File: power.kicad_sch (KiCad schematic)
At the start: 45 parts, among them IC302 L7805, IC303 L7805, J101 Test Points, P302 POWER, Q106 15 29, Q308 FR 32, Q503 BR 29, SW101 SW_SPDT

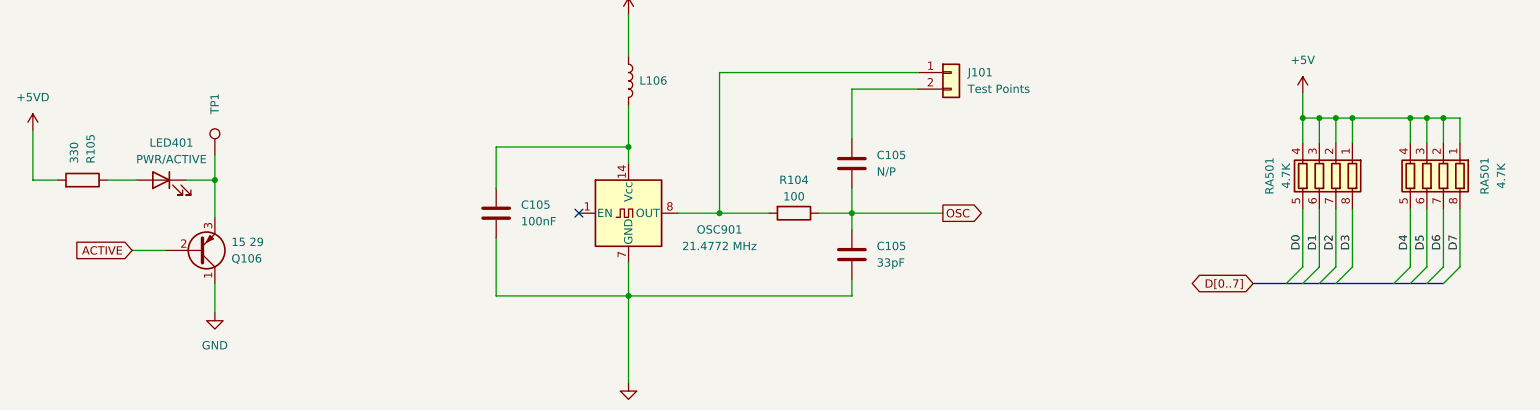
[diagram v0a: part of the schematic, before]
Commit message: Add more capacitor values, rearrange some schematics.
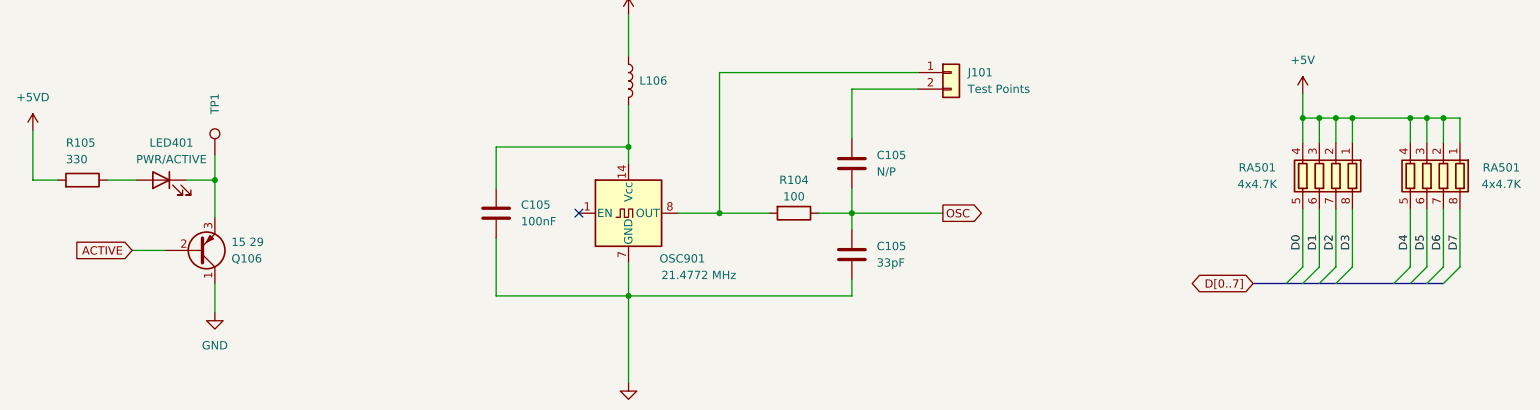
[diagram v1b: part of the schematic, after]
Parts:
- RA501: value 4.7K -> 4x4.7K
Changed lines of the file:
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@@
   (symbol (lib_id "Device:R") (at 42.545 231.775 270) (mirror x) (unit 1)
     (in_bom yes) (on_board yes) (dnp no)
-    (property "Reference" "R105" (at 43.815 229.235 0)
-      (effects (font (size 1.27 1.27)) (justify left))
-    )
-    (property "Value" "330" (at 41.275 229.235 0)
+    (property "Reference" "R105" (at 40.005 226.06 90)
+      (effects (font (size 1.27 1.27)) (justify left))
+    )
+    (property "Value" "330" (at 40.005 228.6 90)
       (effects (font (size 1.27 1.27)) (justify left))
     )
@@
   (symbol (lib_id "Oscillator:CXO_DIP14") (at 126.365 236.855 0) (unit 1)
     (in_bom yes) (on_board yes) (dnp no)
-    (property "Reference" "OSC901" (at 140.335 239.395 0)
-      (effects (font (size 1.27 1.27)))
-    )
-    (property "Value" "21.4772 MHz" (at 140.335 241.935 0)
+    (property "Reference" "OSC901" (at 134.62 243.84 0)
+      (effects (font (size 1.27 1.27)))
+    )
+    (property "Value" "21.4772 MHz" (at 137.16 246.38 0)
       (effects (font (size 1.27 1.27)))
     )
@@
   (symbol (lib_id "Device:R_Pack04") (at 232.41 231.14 180) (unit 1)
     (in_bom yes) (on_board yes) (dnp no)
-    (property "Reference" "RA501" (at 224.79 231.14 90)
-      (effects (font (size 1.27 1.27)))
-    )
-    (property "Value" "4.7K" (at 227.33 231.14 90)
+    (property "Reference" "RA501" (at 222.885 229.87 0)
+      (effects (font (size 1.27 1.27)))
+    )
+    (property "Value" "4x4.7K" (at 222.885 232.41 0)
       (effects (font (size 1.27 1.27)))
     )
@@
   (symbol (lib_id "Device:R_Pack04") (at 248.92 231.14 180) (unit 1)
     (in_bom yes) (on_board yes) (dnp no)
-    (property "Reference" "RA501" (at 257.81 231.14 90)
-      (effects (font (size 1.27 1.27)))
-    )
-    (property "Value" "4.7K" (at 260.35 231.14 90)
-      (effects (font (size 1.27 1.27)))
-    )
+    (property "Reference" "RA501" (at 260.35 229.87 0)
+      (effects (font (size 1.27 1.27)))
+    )
+    (property "Value" "4x4.7K" (at 260.35 232.41 0)
+      (effects (font (size 1.27 1.27)))
+    )

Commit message: Add markings for SMD Ds and Qs.
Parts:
- D501: value ~ -> AV 30
- Q304: value ~ -> BR 30
- ZD302: value ~ -> No Markings
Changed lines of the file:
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@@
       (effects (font (size 1.27 1.27)) (justify left))
     )
-    (property "Value" "~" (at 70.485 146.05 90)
+    (property "Value" "No Markings" (at 70.485 146.05 90)
       (effects (font (size 1.27 1.27)) (justify left))
     )
@@
       (effects (font (size 1.27 1.27)) (justify right))
     )
-    (property "Value" "~" (at 183.515 129.54 90)
+    (property "Value" "AV 30" (at 183.515 129.54 90)
       (effects (font (size 1.27 1.27)) (justify right))
     )
@@
       (effects (font (size 1.27 1.27)) (justify left))
     )
-    (property "Value" "~" (at 97.155 127 0)
-      (effects (font (size 1.27 1.27)) (justify left))
-    )
+    (property "Value" "BR 30" (at 97.155 127 0)
+      (effects (font (size 1.27 1.27)) (justify left))
+    )

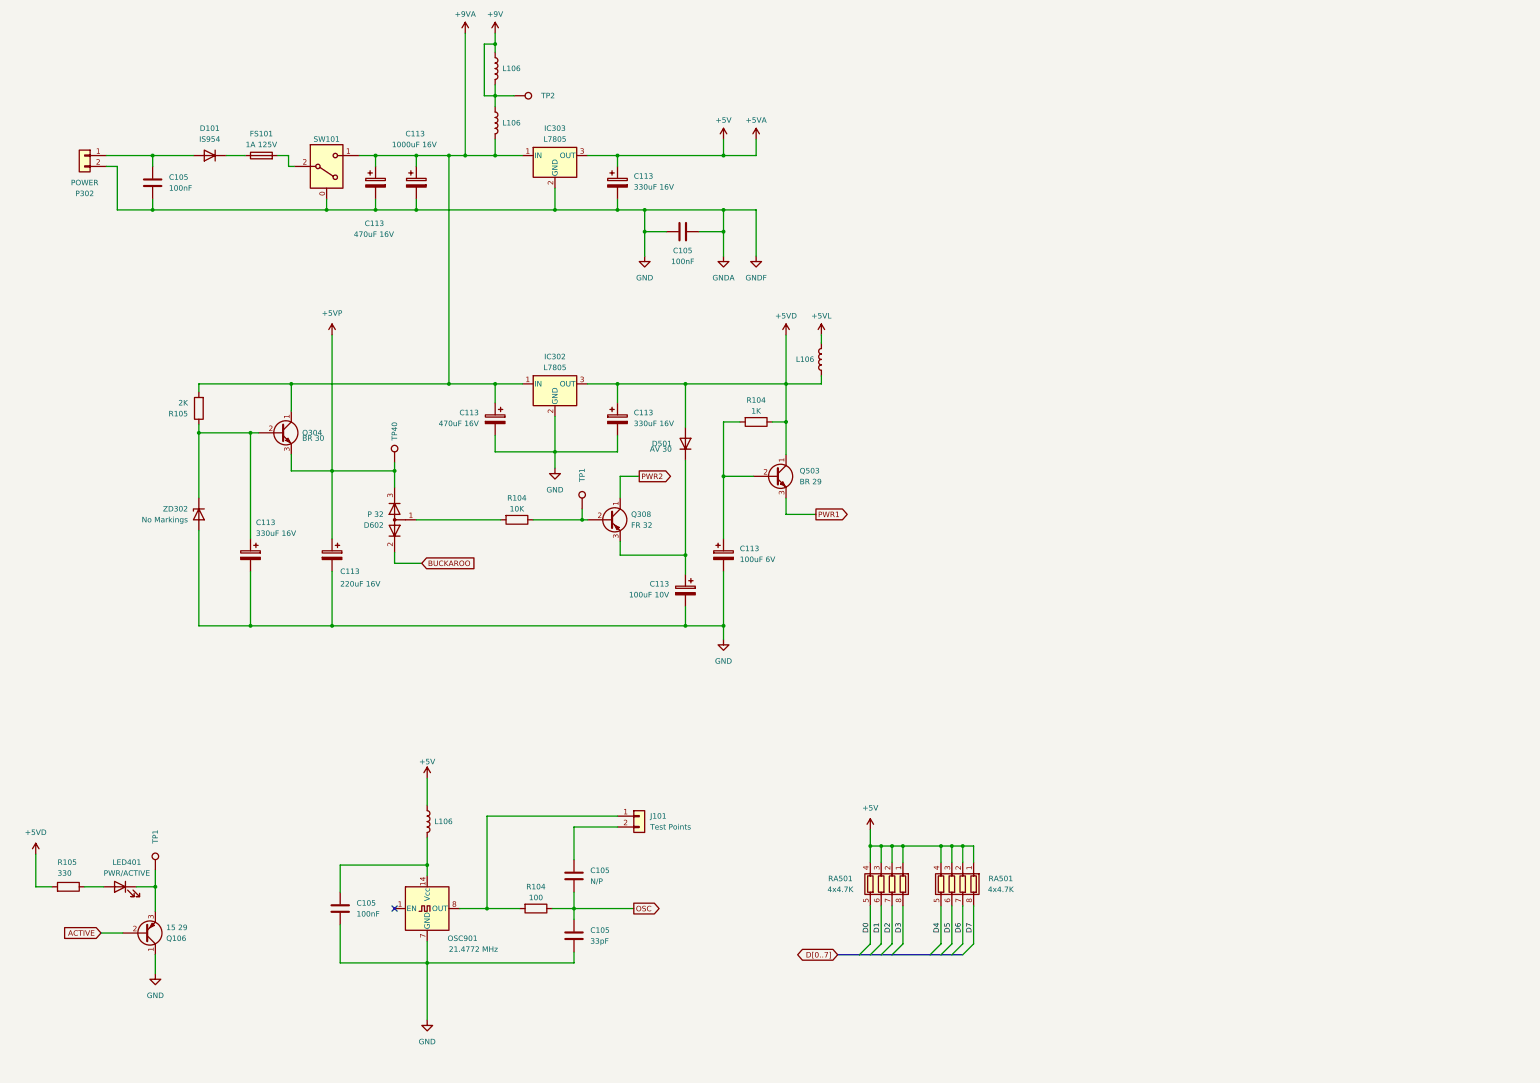
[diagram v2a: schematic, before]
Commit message: More schematic clean-up/annotation.
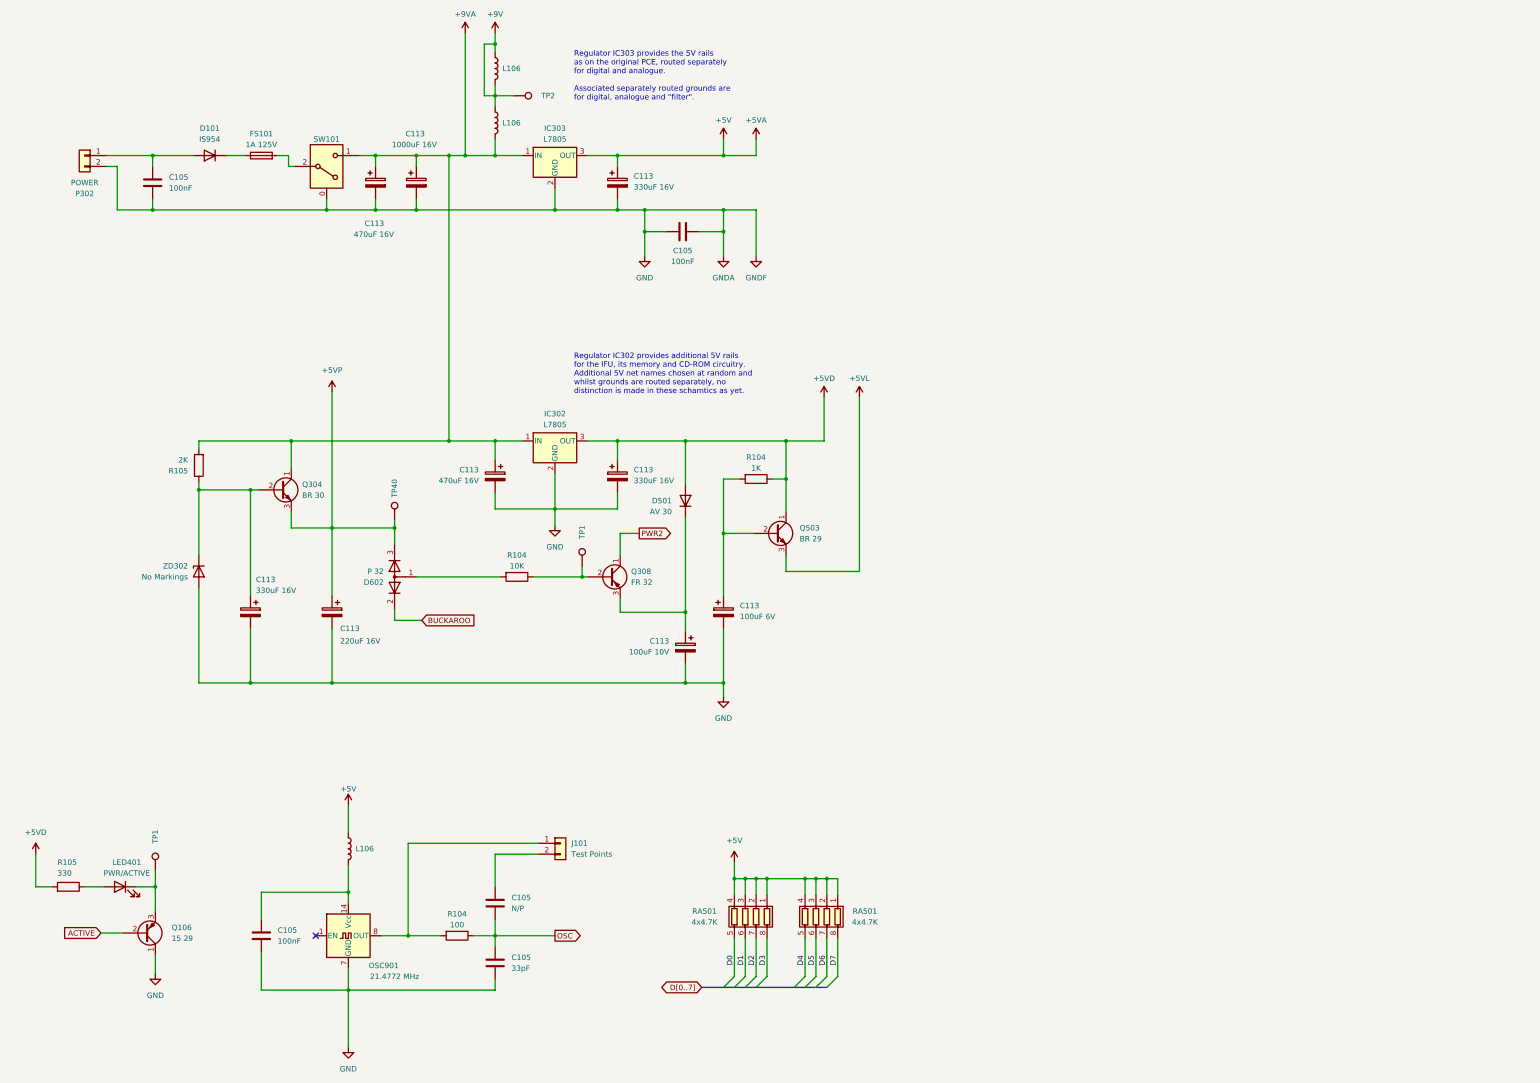
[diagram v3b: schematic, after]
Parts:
- removed L106: ~, A-PCENGINE:SMD_0805_Narrow_Long, symbol Device:L
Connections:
- net PWR1 is gone; now on net +5VL: Q503.3 (E)
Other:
- note added: "Regulator IC302 provides additional 5V rails for the IFU, its memory and CD-ROM circuitry. Additional 5V net names chosen at random and whilst grounds are routed separately, no distinction is made in these schamtics as yet."
- note added: "Regulator IC303 provides the 5V rails as on the original PCE, routed separately for digital and analogue. Associated separately routed grounds are for digital, analogue and "filter"."
- company: (none) -> By Cosam
- title: PC Engine Power, Oscillator and Misc. -> PC Engine Duo Power, Oscillator and Misc.
- moved on the sheet: C105, C113, D501, D602, IC302, J101, L106, OSC901, Q304, Q308, Q503, R104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

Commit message: Minor footprint and silkscreen changes/corrections.
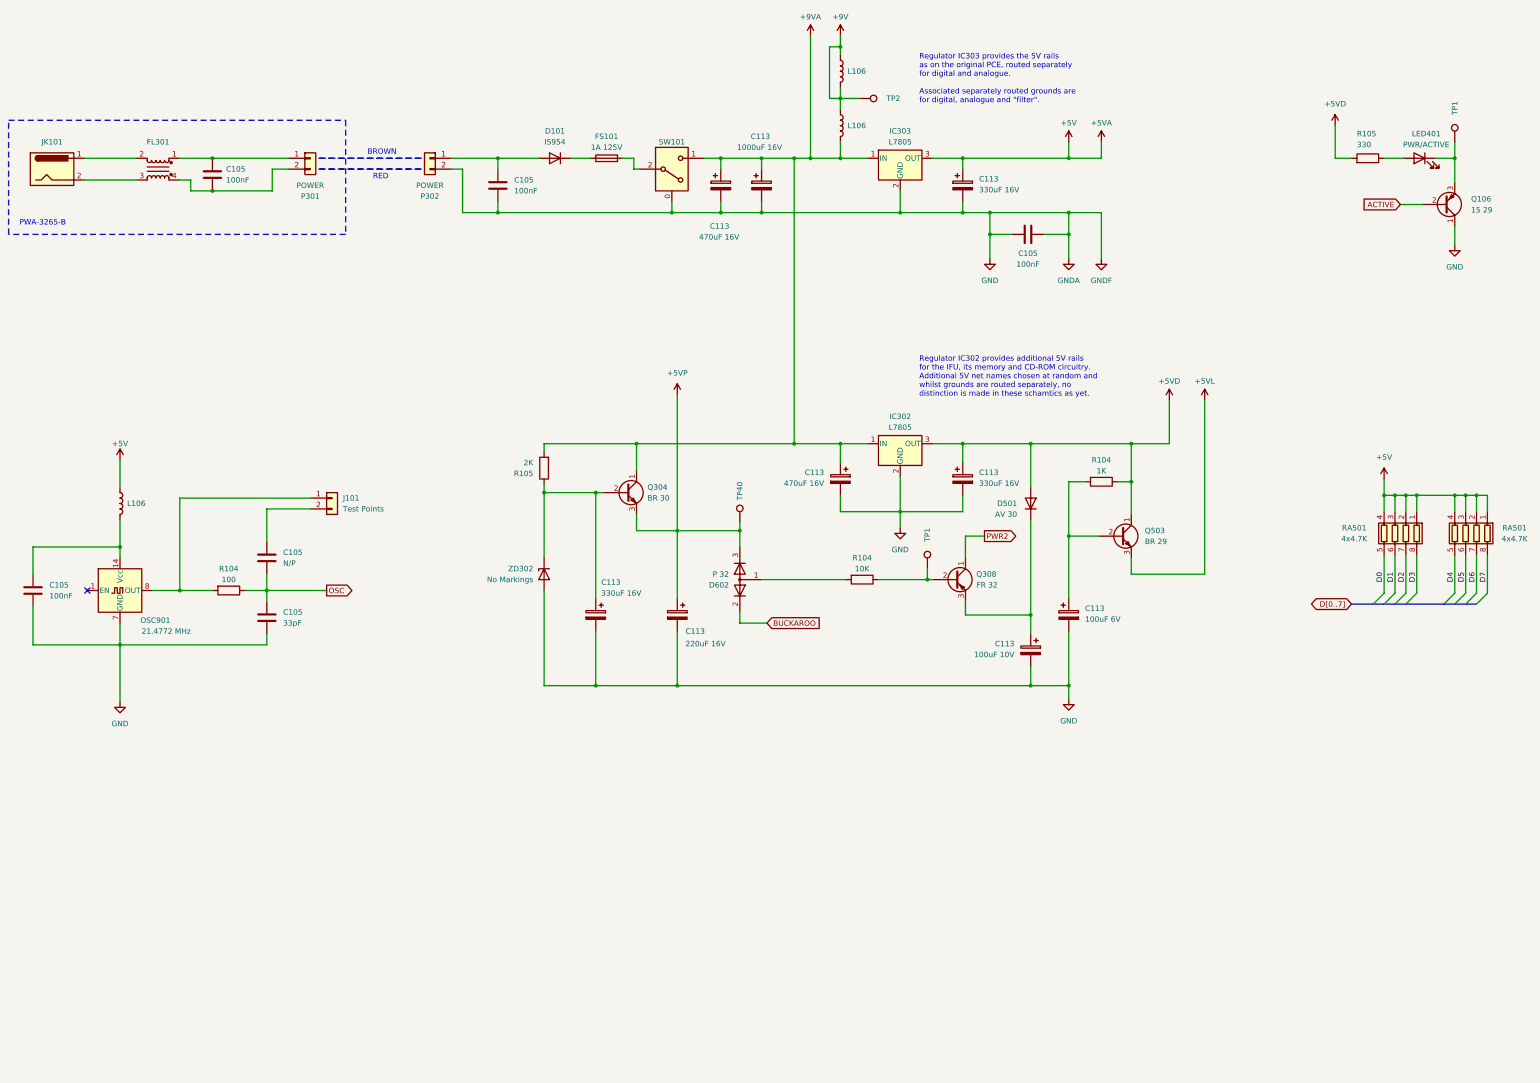
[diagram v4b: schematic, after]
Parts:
- added C105: 100nF, A-PCENGINE:SMD_0805_Narrow, symbol Device:C
- added FL301: ~, symbol PC-Engine:Filter_EMI_LL
- added JK101: Barrel_Jack, symbol Connector:Barrel_Jack
- added P301: POWER, A-PCENGINE:Duo_Power, symbol Connector_Generic:Conn_01x02
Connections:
- new net: C105.1, FL301.1, P301.1 (Pin_1)
- new net: FL301.2, JK101.1
- new net: FL301.3, JK101.2
- new net: C105.2, FL301.4, P301.2 (Pin_2)
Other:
- note added: "BROWN"
- note added: "PWA-3265-B"
- note added: "RED"
- moved on the sheet: C105, C113, D101, D501, D602, FS101, IC302, IC303, J101, L106, LED401, OSC901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
